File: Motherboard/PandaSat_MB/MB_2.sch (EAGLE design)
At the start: 122 parts, among them J1 503182-1852, J10 1445055-5, J2 10118194-0001LF, J3 DCJ0303, J4 1445055-5, J5 1445055-5, J6 1445055-5, J7 BK-18650, J8 1445055-5, J9 1445055-5, Q10 IRLML5103, Q11 IRLML5103, Q13 IRLML2803, Q14 IRLML2803, Q15 IRLML2803, Q16 IRLML5103, Q17 2N5088, Q2 32.768, U1 MAX706R, U11 DRV8848, U12 DRV8848, U13 DRV8848, U2 LTC4121-4.2, U3 LSM9DS1, U4 PE014006, U5 MAX4372TEUK+T, U6 RFM23BP, U7 TPS54226PWPRPWP14_2P31X2P46-L, U8 ATSAMD51, U9 OKL-T3-W12, X1 BU-SMA-V

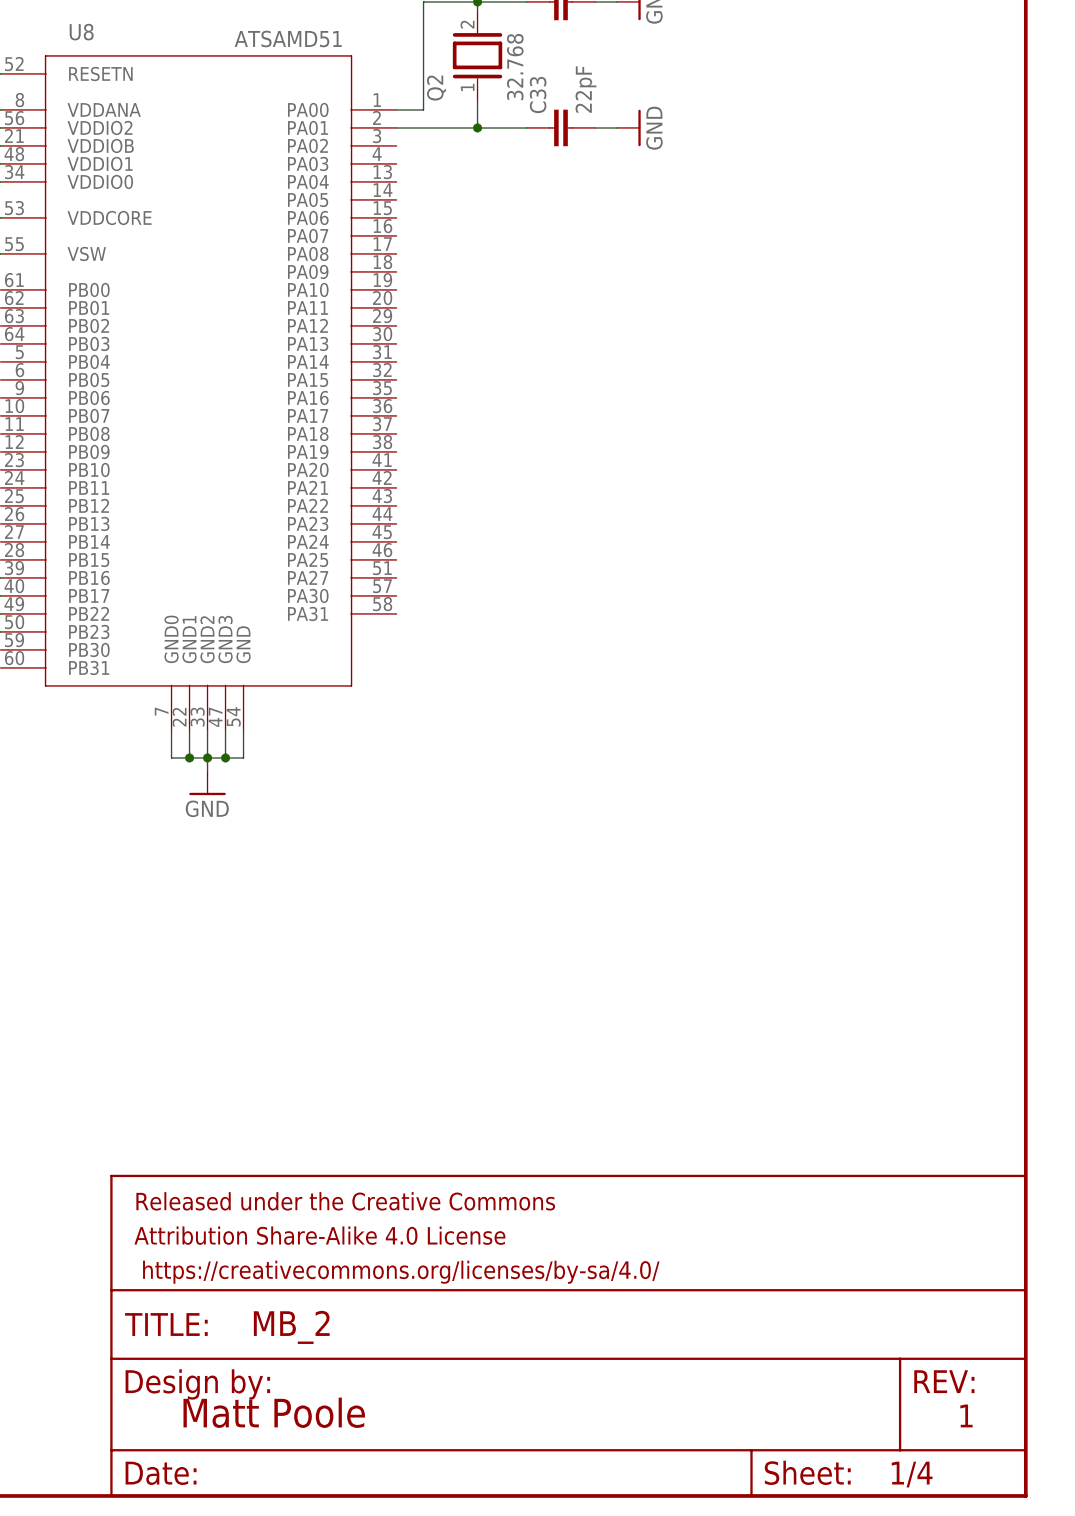
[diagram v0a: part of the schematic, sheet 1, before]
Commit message: Added I2C and WDT Interface
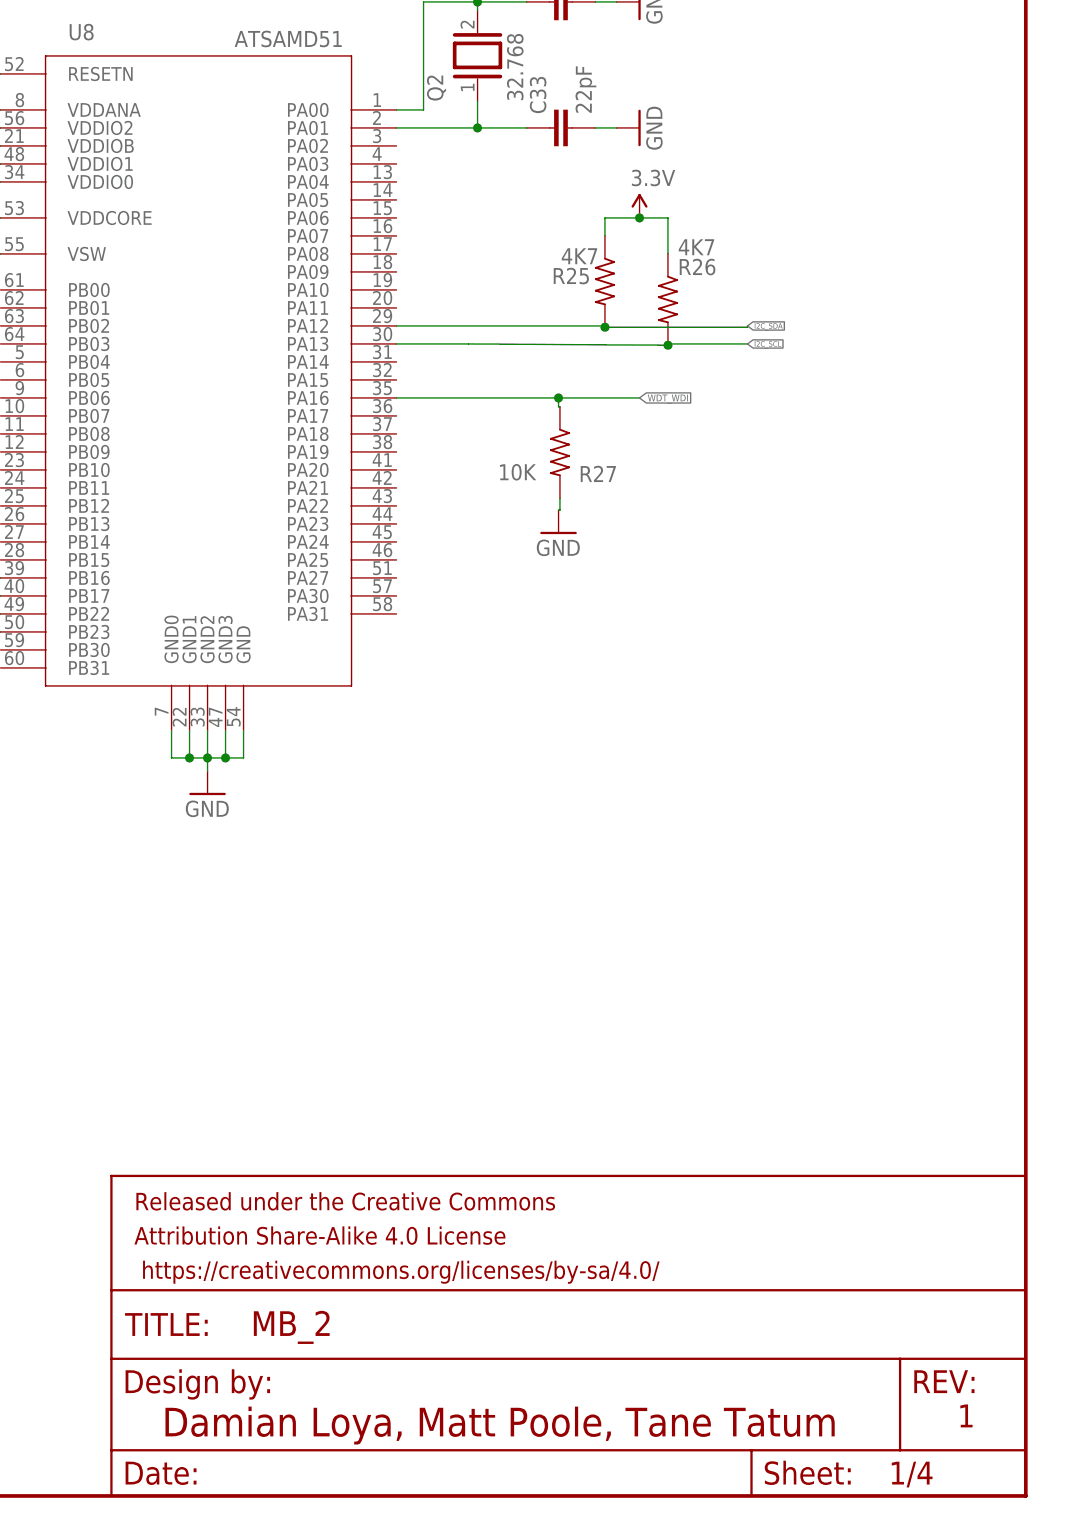
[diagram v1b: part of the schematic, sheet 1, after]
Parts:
- added R25, R26: 4K7, resistor:R-US_R0603
- added R27: 10K, resistor:R-US_R0603
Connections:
- net 3.3V: now also R25.1, R26.1
- net GND: now also R27.2
- net I2C_SCL: now also R26.2, U8.PA13
- net I2C_SDA: now also R25.2, U8.PA12
- net WDT_WDI: now also R27.1, U8.PA16
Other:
- note added: "Damian Loya, Matt Poole, Tane Tatum"
- note removed: "Matt Poole"
- note removed: "Zac Manchester, Max Holliday"
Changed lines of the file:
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@@
 <setting verticaltext="up"/>
 </settings>
-<grid distance="0.01" unitdist="inch" unit="inch" style="lines" multiple="1" display="yes" altdistance="0.01" altunitdist="inch" altunit="inch"/>
+<grid distance="1" unitdist="mm" unit="mm" style="lines" multiple="1" display="yes" altdistance="0.01" altunitdist="inch" altunit="inch"/>
 <layers>
 <layer number="1" name="Top" color="35" fill="1" visible="no" active="no"/>
@@
 <part name="GND40" library="supply1" library_urn="urn:adsk.eagle:library:371" deviceset="GND" device=""/>
 <part name="D4" library="BrownSpaceEngineering" deviceset="DFLS130L" device="" value="DFLS130L"/>
+<part name="R25" library="resistor" library_urn="urn:adsk.eagle:library:348" deviceset="R-US_" device="R0603" package3d_urn="urn:adsk.eagle:package:26057/1" value="4K7"/>
+<part name="R26" library="resistor" library_urn="urn:adsk.eagle:library:348" deviceset="R-US_" device="R0603" package3d_urn="urn:adsk.eagle:package:26057/1" value="4K7"/>
+<part name="SUPPLY15" library="SparkFun-Aesthetics" deviceset="3.3V" device=""/>
+<part name="R27" library="resistor" library_urn="urn:adsk.eagle:library:348" deviceset="R-US_" device="R0603" package3d_urn="urn:adsk.eagle:package:26057/1" value="10K"/>
+<part name="GND41" library="supply1" library_urn="urn:adsk.eagle:library:371" deviceset="GND" device=""/>
 </parts>
 <sheets>
@@
 <description>Avionics</description>
 <plain>
-<text x="154.94" y="7.62" size="3.175" layer="94">Matt Poole</text>
 <text x="241.3" y="7.62" size="2.54" layer="94">1</text>
 <text x="93.98" y="50.8" size="2.54" layer="98" align="top-left">To Do:
@@
 <text x="15.24" y="53.34" size="2.54" layer="97" align="top-left">HopeRF RFM23B module at 5V</text>
 <text x="131.94" y="179.8" size="2.54" layer="97">SAM51 MCU</text>
+<text x="152.94" y="6.62" size="3.175" layer="94">Damian Loya, Matt Poole, Tane Tatum</text>
 </plain>
 <instances>
@@
 <instance part="GND40" gate="1" x="206" y="152" smashed="yes" rot="R90">
 <attribute name="VALUE" x="208.54" y="149.46" size="1.778" layer="96" rot="R90"/>
+</instance>
+<instance part="R25" gate="G$1" x="202.16" y="134.94" smashed="yes" rot="R270">
+<attribute name="NAME" x="196.25" y="134.6586" size="1.778" layer="95"/>
+<attribute name="VALUE" x="197.25" y="136.858" size="1.778" layer="96"/>
+</instance>
+<instance part="R26" gate="G$1" x="209.16" y="132.94" smashed="yes" rot="R270">
+<attribute name="NAME" x="210.25" y="135.6586" size="1.778" layer="95"/>
+<attribute name="VALUE" x="210.25" y="137.858" size="1.778" layer="96"/>
+</instance>
+<instance part="SUPPLY15" gate="G$1" x="206" y="142" smashed="yes">
+<attribute name="VALUE" x="204.984" y="145.556" size="1.778" layer="96"/>
+</instance>
+<instance part="R27" gate="G$1" x="197.16" y="115.94" smashed="yes" rot="R270">
+<attribute name="NAME" x="199.25" y="112.6586" size="1.778" layer="95"/>
+<attribute name="VALUE" x="190.25" y="112.858" size="1.778" layer="96"/>
+</instance>
+<instance part="GND41" gate="1" x="197" y="107" smashed="yes">
+<attribute name="VALUE" x="194.46" y="104.46" size="1.778" layer="96"/>
 </instance>
 </instances>
@@
 <wire x1="201.08" y1="152" x2="203.46" y2="152" width="0.1524" layer="91"/>
 </segment>
+<segment>
+<pinref part="GND41" gate="1" pin="GND"/>
+<pinref part="R27" gate="G$1" pin="2"/>
+<wire x1="197" y1="109.54" x2="197.16" y2="109.54" width="0.1524" layer="91"/>
+<wire x1="197.16" y1="109.54" x2="197.16" y2="110.86" width="0.1524" layer="91"/>
+</segment>
 </net>
 <net name="3.3V" class="0">
@@
 <wire x1="110" y1="171" x2="110" y2="169.08" width="0.1524" layer="91"/>
 </segment>
+<segment>
+<pinref part="R25" gate="G$1" pin="1"/>
+<pinref part="SUPPLY15" gate="G$1" pin="3.3V"/>
+<wire x1="202.16" y1="140.02" x2="202.16" y2="142" width="0.1524" layer="91"/>
+<wire x1="202.16" y1="142" x2="206" y2="142" width="0.1524" layer="91"/>
+<pinref part="R26" gate="G$1" pin="1"/>
+<wire x1="206" y1="142" x2="209.16" y2="142" width="0.1524" layer="91"/>
+<wire x1="209.16" y1="142" x2="209.16" y2="138.02" width="0.1524" layer="91"/>
+<junction x="206" y="142"/>
+</segment>
 </net>
 <net name="I2C_SCL" class="0">
@@
 <wire x1="66.04" y1="114.3" x2="68.58" y2="114.3" width="0.1524" layer="91"/>
 </segment>
+<segment>
+<pinref part="U8" gate="G$1" pin="PA13"/>
+<wire x1="179" y1="128" x2="187" y2="128" width="0.1524" layer="91"/>
+<label x="218" y="128" size="0.6096" layer="95" xref="yes"/>
+<pinref part="R26" gate="G$1" pin="2"/>
+<wire x1="187" y1="128" x2="209.16" y2="127.86" width="0.1524" layer="91"/>
+<wire x1="209.16" y1="127.86" x2="209.16" y2="128" width="0.1524" layer="91"/>
+<wire x1="209.16" y1="128" x2="218" y2="128" width="0.1524" layer="91"/>
+<junction x="209.16" y="127.86"/>
+</segment>
 </net>
 <net name="I2C_SDA" class="0">
@@
 <wire x1="63.5" y1="116.84" x2="63.5" y2="111.76" width="0.1524" layer="91"/>
 <wire x1="63.5" y1="116.84" x2="68.58" y2="116.84" width="0.1524" layer="91"/>
+</segment>
+<segment>
+<pinref part="U8" gate="G$1" pin="PA12"/>
+<label x="218" y="130" size="0.6096" layer="95" xref="yes"/>
+<pinref part="R25" gate="G$1" pin="2"/>
+<wire x1="179" y1="130" x2="202.16" y2="130" width="0.1524" layer="91"/>
+<wire x1="202.16" y1="130" x2="202.16" y2="129.86" width="0.1524" layer="91"/>
+<wire x1="202.16" y1="129.86" x2="218" y2="129.86" width="0.1524" layer="91"/>
+<wire x1="218" y1="129.86" x2="218" y2="130" width="0.1524" layer="91"/>
+<junction x="202.16" y="129.86"/>
 </segment>
 </net>
@@
 <label x="27.94" y="144.78" size="1.27" layer="95" rot="R180" xref="yes"/>
 <wire x1="27.94" y1="144.78" x2="30.48" y2="144.78" width="0.1524" layer="91"/>
+</segment>
+<segment>
+<pinref part="U8" gate="G$1" pin="PA16"/>
+<wire x1="179" y1="122" x2="197" y2="122" width="0.1524" layer="91"/>
+<label x="206" y="122" size="0.75" layer="95" xref="yes"/>
+<pinref part="R27" gate="G$1" pin="1"/>
+<wire x1="197" y1="122" x2="206" y2="122" width="0.1524" layer="91"/>
+<wire x1="197.16" y1="121.02" x2="197" y2="121.02" width="0.1524" layer="91"/>
+<wire x1="197" y1="121.02" x2="197" y2="122" width="0.1524" layer="91"/>
+<junction x="197" y="122"/>
 </segment>
 </net>
@@
 <plain>
 <text x="30.48" y="66.04" size="1.778" layer="97">Battery Current Sensor</text>
-<text x="154.94" y="7.62" size="3.175" layer="94">Matt Poole</text>
 <text x="193.04" y="76.2" size="2.54" layer="95">Payload Power</text>
 <wire x1="147.32" y1="35.56" x2="147.32" y2="81.28" width="0.2032" layer="97" style="longdash"/>
@@
 Ichrg=988*Vprog/Rprog
 </text>
+<text x="153.94" y="6.62" size="3.175" layer="94">Damian Loya, Matt Poole, Tane Tatum</text>
 </plain>
 <instances>
@@
 <description>Connectors</description>
 <plain>
-<text x="154.94" y="7.62" size="3.175" layer="94">Zac Manchester, Max Holliday</text>
+<text x="154.94" y="7.62" size="3.175" layer="94">Damian Loya, Matt Poole, Tane Tatum</text>
 <text x="241.3" y="7.62" size="2.54" layer="94">5</text>
 <text x="33.274" y="81.788" size="2.54" layer="97" align="top-left">JTAG</text>
@@
 <text x="113.284" y="177.292" size="2.54" layer="97">Burn Wire Control (Antenna Depolyment)</text>
 <text x="108.204" y="117.856" size="2.54" layer="91">H-Bridges</text>
+<text x="156.94" y="6.62" size="3.175" layer="94">Damian Loya, Matt Poole, Tane Tatum</text>
 </plain>
 <instances>
